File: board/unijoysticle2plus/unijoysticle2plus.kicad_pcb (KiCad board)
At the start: 2 copper layers, 35 parts, among them J1 DB9_Female, J2 DB9_Female, J3 Barrel_Jack, J4 Conn_01x03_Male, J5 USB_B_Micro, Q1 S8050, Q2 S8050, SW1 SW_Push, SW2 SW_SPST, SW3 SW_Push, SW4 SW_Push, U1 ESP32-WROOM-32D, U2 74LS05, U3 74LS05, U4 CP2102N-A01-GQFN24, U5 AP2114H-3_3TRG1

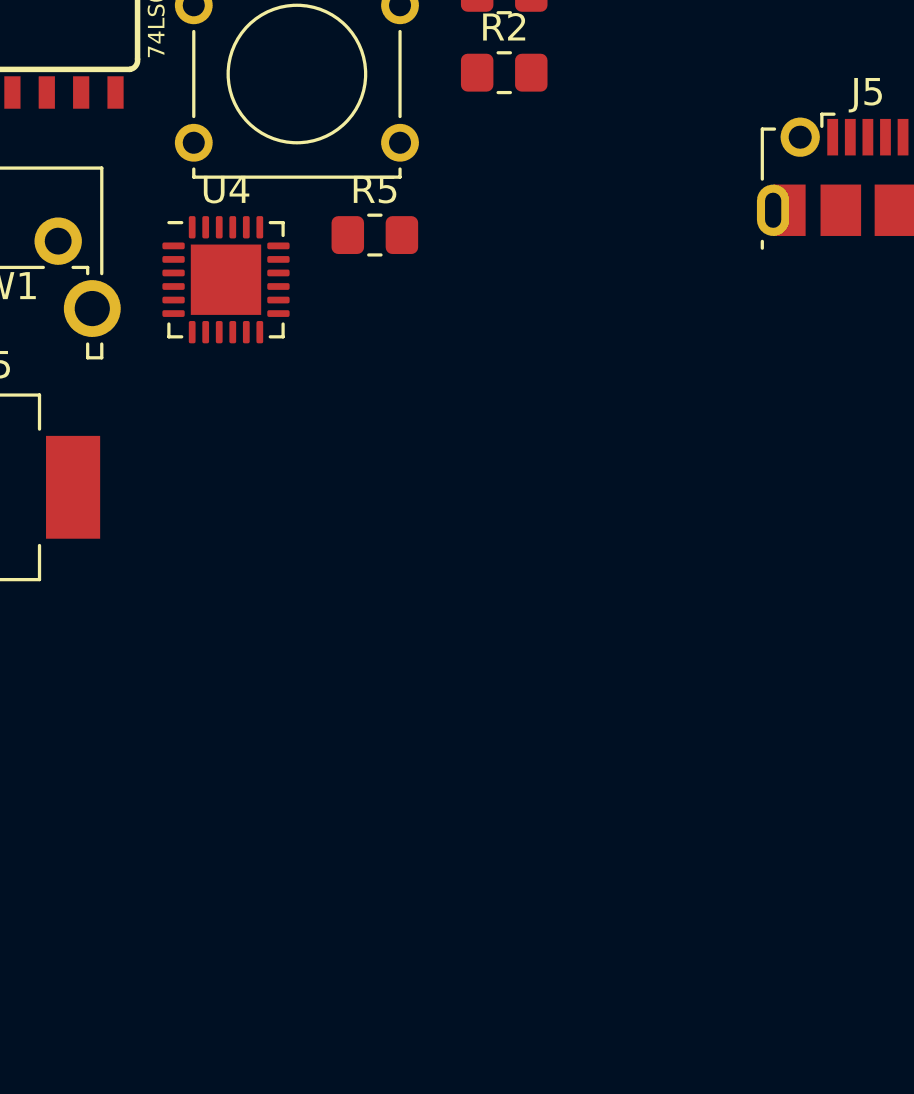
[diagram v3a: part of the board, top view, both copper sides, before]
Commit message: Firmware cleanup: remove obsolte files
Remove Changelog/License related to firmware
Remove code files from .gitignore
  Ignore fp-info-cache (kicad  file)
Update docs like pair_ds3 which points to Bluepad32

Regarding Unijoysticle2Plus: non important changes... this is still
pretty much WIP, so just ignore these changes
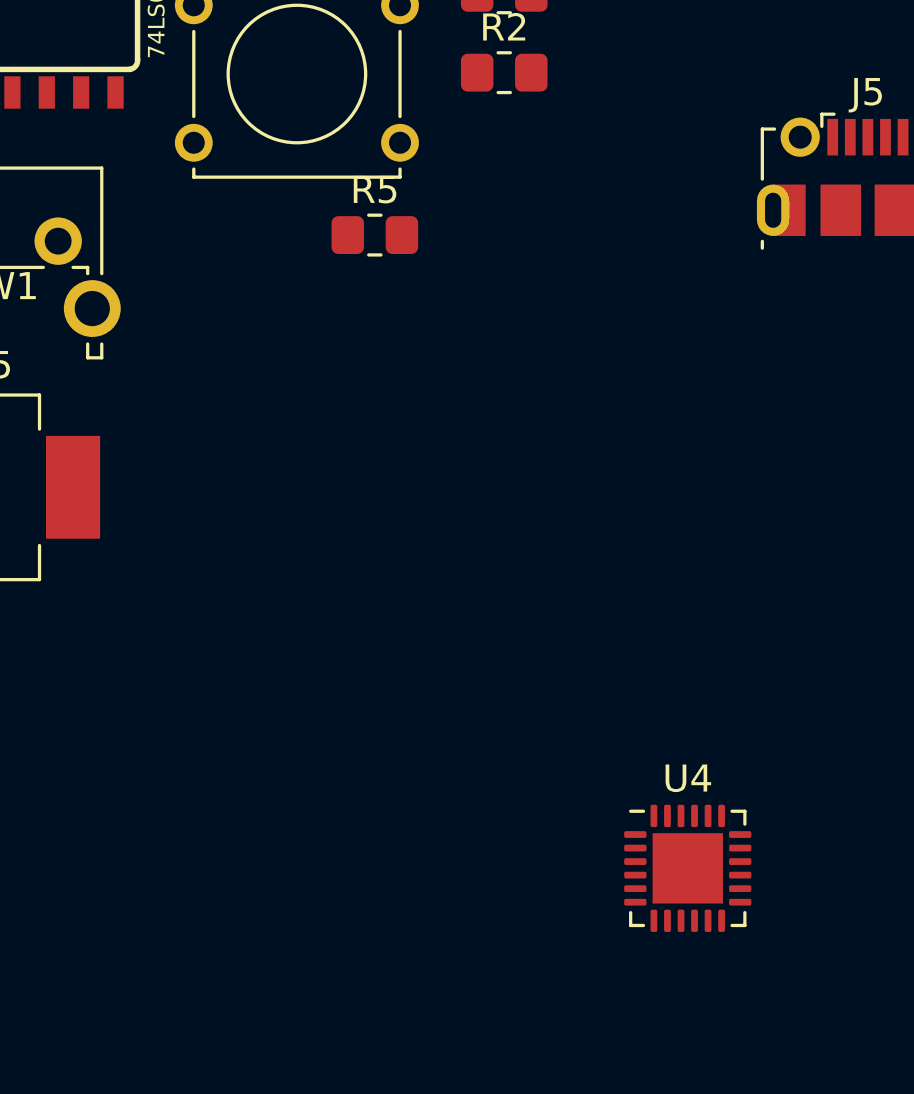
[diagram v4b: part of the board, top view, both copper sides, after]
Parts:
- moved U4 27.6 mm to (139.2, -14.2)

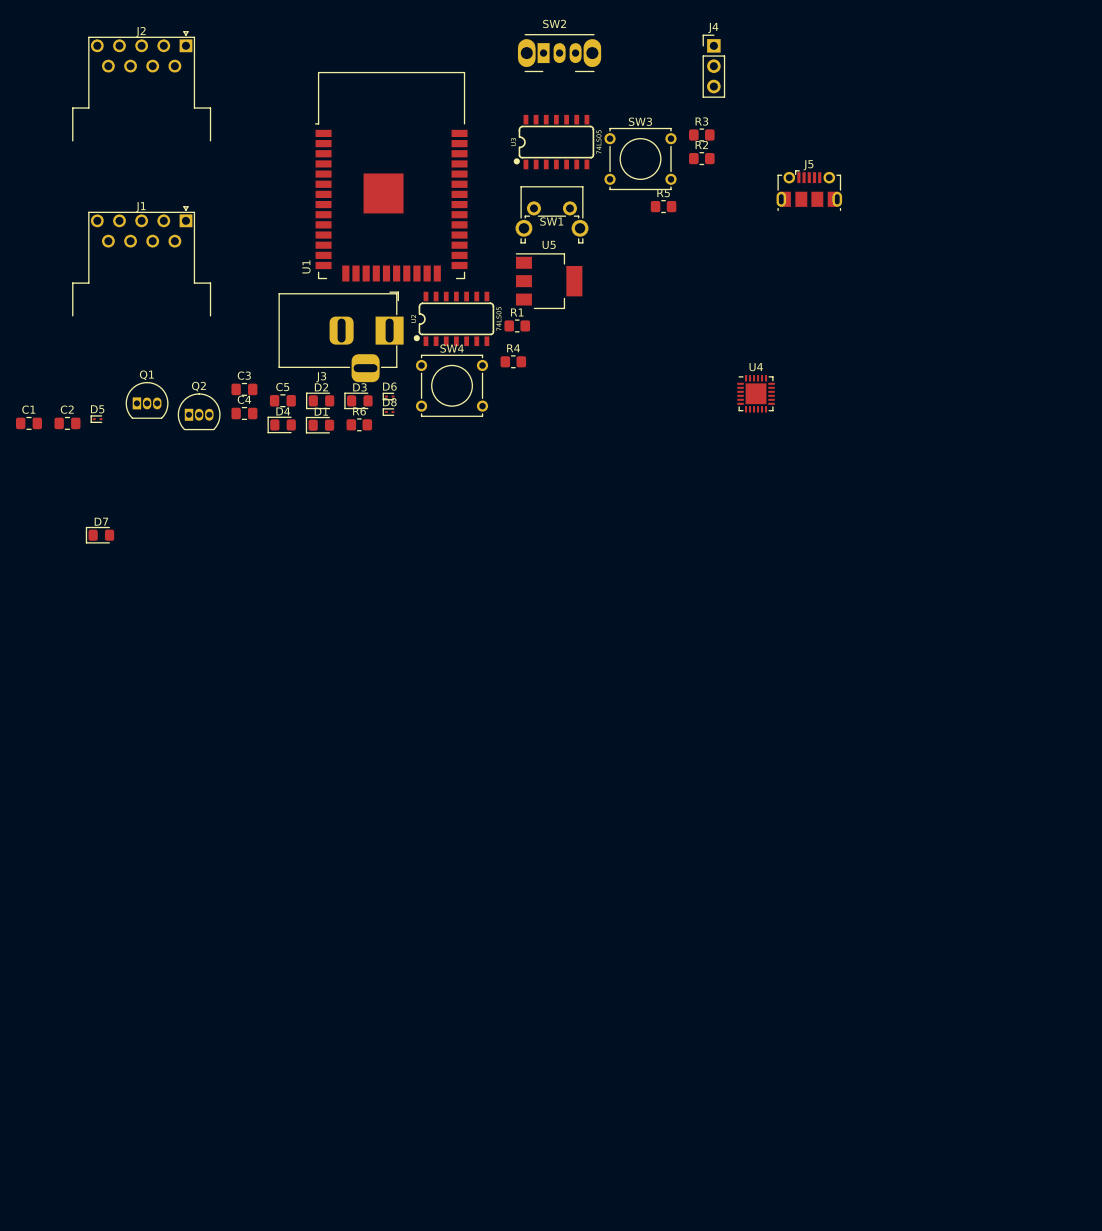
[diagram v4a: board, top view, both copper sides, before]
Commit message: unijoysticle2 plus: using ch340c (WIP)
After researching which could be the cheapest way to create a board that
could be assembled by JLCPCB, it seems that using CH340C is the way to
go:

- CH340C is an extended part, but doesn't require oscillator. Cost: $0.5
- CH340G is a basic part, but requires 12Mhz oscillar, which is an
  external part.
- CP210x, are all external parts and cost > $2

So, the design will include a CH340C.

Schematic is "ready", but layout is not.
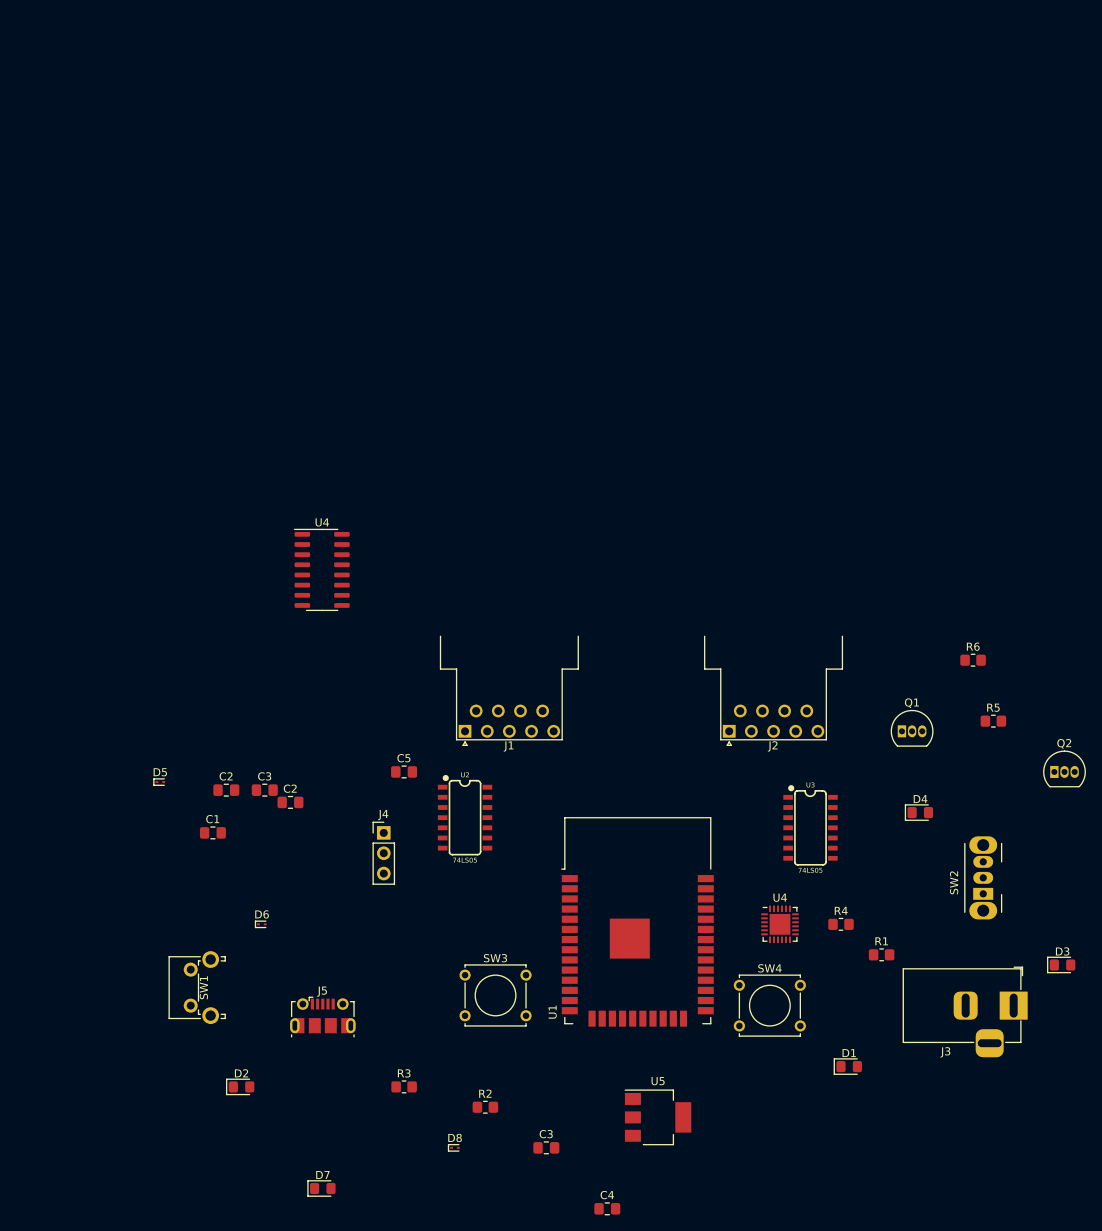
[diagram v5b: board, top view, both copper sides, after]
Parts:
- added C2: .1uF, Capacitor_SMD:C_0805_2012Metric_Pad1.18x1.45mm_HandSolder, F.Cu at (73.0, 35.3)
- added C3: .1uF, Capacitor_SMD:C_0805_2012Metric_Pad1.18x1.45mm_HandSolder, F.Cu at (77.8, 35.3)
- added U4: CH340C, Package_SO:SOIC-16_3.9x9.9mm_P1.27mm, F.Cu at (85.0, 7.77)
- moved R3 124.7 mm to (95.2, 72.4)
- moved R2 121.6 mm to (105.4, 74.9)
- moved J5 119.9 mm to (85.1, 63.5)
- moved SW2 118.6 mm to (167.6, 48.3), turned to 90 degrees
- moved Q2 117.0 mm to (176.5, 33.0)
- moved J3 114.9 mm to (171.4, 62.2)
- moved D3 112.6 mm to (177.6, 57.1)
- moved J2 109.3 mm to (135.9, 27.9), turned to 180 degrees
- moved C4 109.3 mm to (120.7, 87.6)
- moved SW1 108.5 mm to (68.6, 62.2), turned to 90 degrees
- moved J4 106.7 mm to (92.7, 40.6)
- moved SW3 106.1 mm to (102.9, 58.4)
- moved U5 105.4 mm to (127.0, 76.2)
- moved Q1 104.0 mm to (157.5, 27.9)
- moved D1 103.8 mm to (150.9, 69.8)
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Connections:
- C1 pad 2: GND -> +5V
- C4 pad 2: GND -> +5V
- C5 pad 2: GND -> +5V
- D1 pad 1: GND -> +5V
- D2 pad 1: GND -> +5V
- D5 pad 1: GND -> +5V
- D6 pad 1: GND -> +5V
- D6 pad 2: /USB_DP -> /USBD+
- D8 pad 1: GND -> +5V
- D8 pad 2: /USB_DN -> /USBD-
- J1 pad 5: (no net) -> /J1_POTY
- J1 pad 8: GND -> +5V
- J1 pad 9: (no net) -> /J1_POTX
- J2 pad 5: (no net) -> /J2_POTY
- J2 pad 8: GND -> +5V
- J2 pad 9: (no net) -> /J2_POTX
- J3 pad 2: GND -> +5V
- J5 pad 2: /USB_DN -> /USBD-
- J5 pad 3: /USB_DP -> /USBD+
- J5 pad 4: (no net) -> Net-(J5-Pad4)
- J5 pad 5: GND -> +5V
- J5 pad 6: GND -> +5V
- Q1 pad 3: (no net) -> /BOOT
- SW1 pad 1: GND -> +5V
- SW3 pad 1: GND -> +5V
- SW4 pad 2: GND -> +5V
- U1 pad 1: GND -> +5V
- U1 pad 15: GND -> +5V
- U1 pad 17: (no net) -> Net-(U1-Pad17)
- U1 pad 18: (no net) -> Net-(U1-Pad18)
- U1 pad 19: (no net) -> Net-(U1-Pad19)
- U1 pad 20: (no net) -> Net-(U1-Pad20)
- U1 pad 21: (no net) -> Net-(U1-Pad21)
- U1 pad 22: (no net) -> Net-(U1-Pad22)
- U1 pad 24: (no net) -> Net-(U1-Pad24)
- U1 pad 27: (no net) -> /GPIO_J1_POTY
- U1 pad 32: (no net) -> Net-(U1-Pad32)
- U1 pad 33: (no net) -> /GPIO_J2_POTX
- U1 pad 34: /RXD -> /ESP_RXD
- U1 pad 35: /TXD -> /ESP_TXD
- U1 pad 36: (no net) -> /GPIO_J2_POTY
- U1 pad 38: GND -> +5V
- U1 pad 39: GND -> +5V
- U1 pad 4: (no net) -> Net-(U1-Pad4)
- U1 pad 5: (no net) -> Net-(U1-Pad5)
- U1 pad 9: (no net) -> /GPIO_J1_POTX
- U2 pad 12: (no net) -> Net-(U2-Pad12)
- U2 pad 13: (no net) -> Net-(U2-Pad13)
- U2 pad 7: GND -> +5V
- U3 pad 12: (no net) -> Net-(U3-Pad12)
- U3 pad 13: (no net) -> Net-(U3-Pad13)
- U3 pad 7: GND -> +5V
- U5 pad 1: GND -> +5V

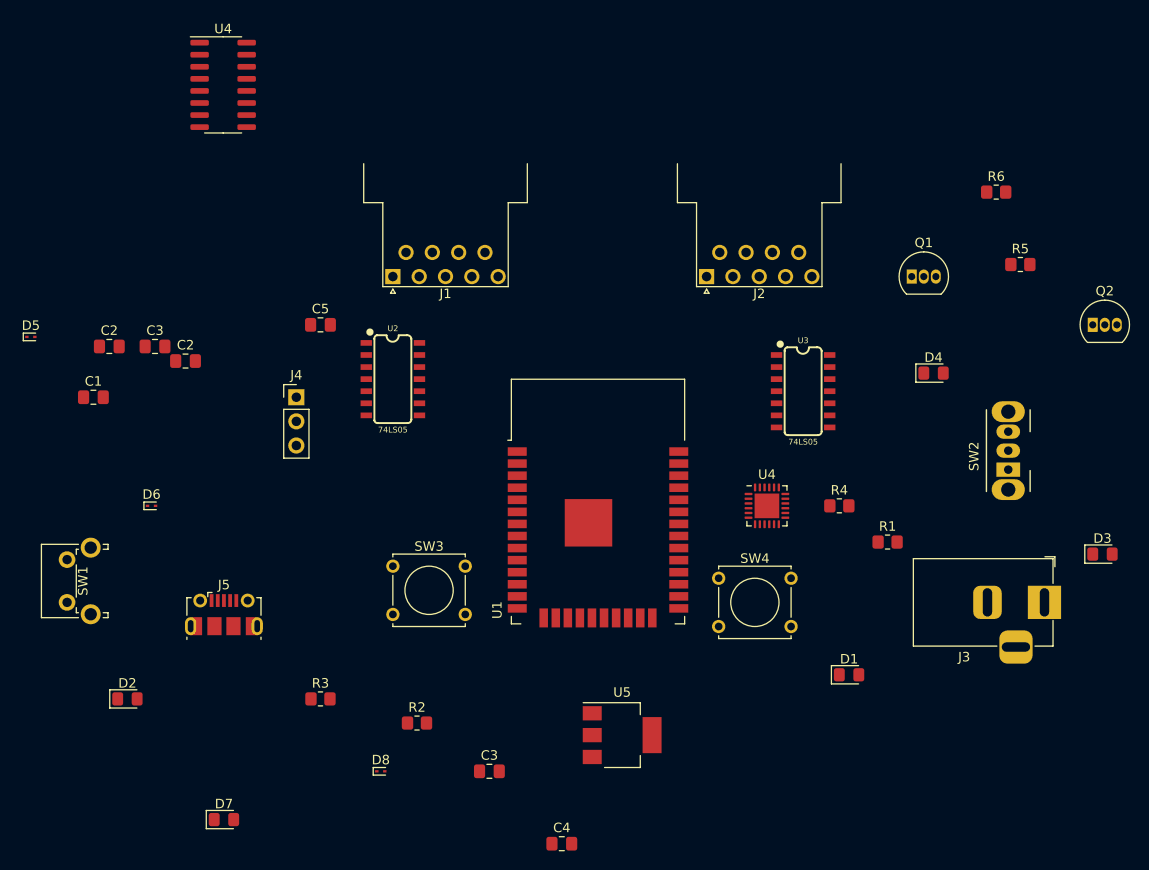
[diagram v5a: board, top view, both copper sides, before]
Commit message: unijoysticle2plus: auto-reset circuit fixed and minor fixes
Transistor had B/E/C wrong.
Correct package for push buttons for reset & boot.
Improved package for 7405 (renamed it from 74lc05 to 74hc05).

Reset layout. Not working on it yet since schematic is not ready yet
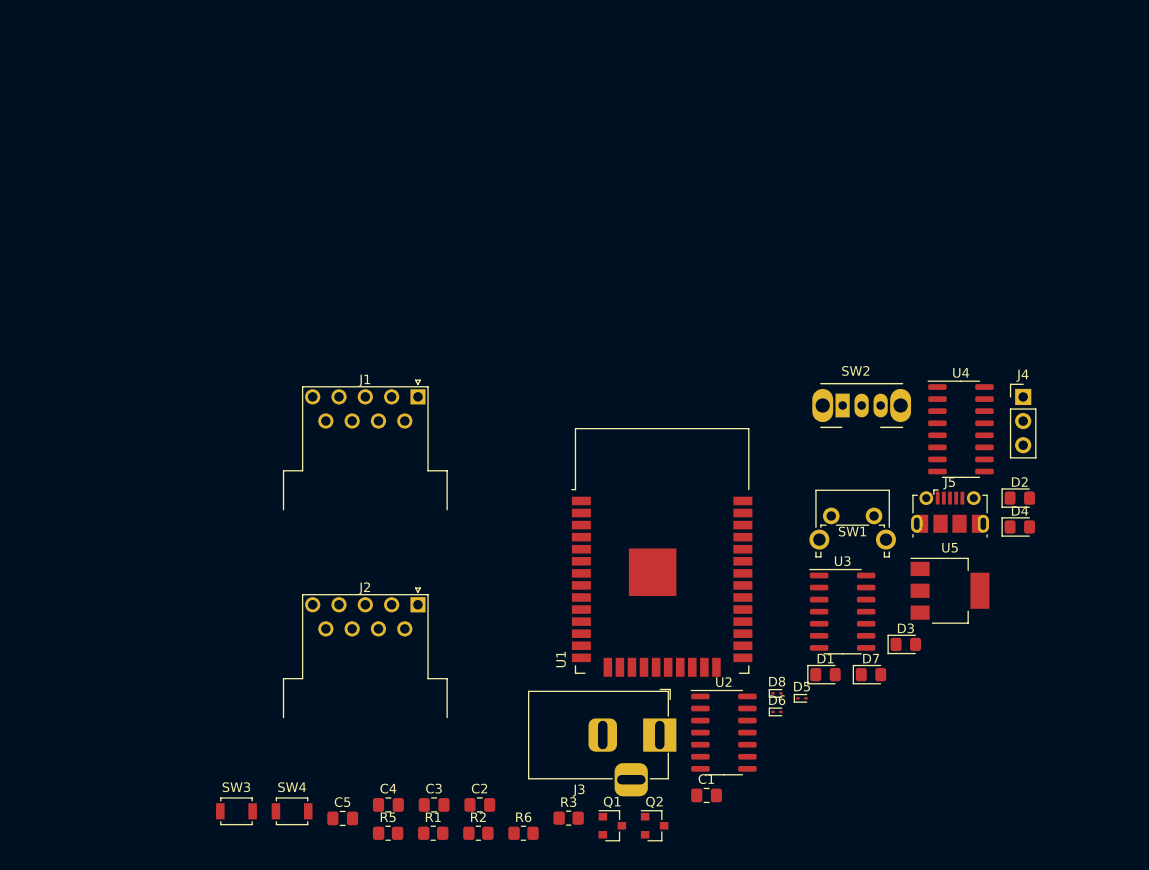
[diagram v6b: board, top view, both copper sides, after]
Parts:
- removed the C2 at (73.0, 35.3)
- removed the C2 at (81.0, 36.8)
- removed the C3 at (77.8, 35.3)
- removed the C3 at (113.0, 80.0)
- removed R4: 1k, Resistor_SMD:R_0805_2012Metric_Pad1.20x1.40mm_HandSolder
- removed the U4 at (85.0, 7.77)
- removed the U4 at (142.2, 52.1)
- added C2: .1uF, Capacitor_SMD:C_0805_2012Metric_Pad1.18x1.45mm_HandSolder, F.Cu at (112.0, 83.5)
- added C3: .1uF, Capacitor_SMD:C_0805_2012Metric_Pad1.18x1.45mm_HandSolder, F.Cu at (107.2, 83.5)
- added U4: CH340C, Package_SO:SOIC-16_3.9x9.9mm_P1.27mm, F.Cu at (162.7, 44.0)
- Q1, Q2: value S8050 -> MMSS8050-H-TP; footprint Package_TO_SOT_THT:TO-92_Inline -> Package_TO_SOT_SMD:SOT-23
- SW3, SW4: footprint Button_Switch_THT:SW_Tactile_Straight_KSA0Axx1LFTR -> Button_Switch_SMD:SW_SPST_B3U-1000P
- U2, U3: footprint Silicon-Standard:SO14 -> Package_SO:SOIC-14_3.9x8.7mm_P1.27mm
- moved D2 96.3 mm to (168.9, 51.3)
- moved D5 89.6 mm to (145.9, 72.3)
- moved R5 89.5 mm to (102.4, 86.5)
- moved R6 83.8 mm to (116.6, 86.5)
- moved SW1 80.9 mm to (149.0, 53.1), turned to 0 degrees
- moved J5 77.2 mm to (161.5, 52.7)
- moved C1 77.0 mm to (135.9, 82.5)
- moved J4 76.5 mm to (169.2, 40.6)
- moved Q2 70.0 mm to (130.4, 85.7)
- moved D7 69.8 mm to (153.2, 69.8)
- moved D6 69.3 mm to (143.3, 73.8)
- moved Q1 65.8 mm to (126.0, 85.7)
- moved R1 56.8 mm to (107.1, 86.5)
- moved C5 52.0 mm to (97.6, 85.0)
- moved U2 51.4 mm to (137.7, 75.9), turned to 0 degrees
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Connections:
- C1 pad 1: /RESET -> /ESP_RESET
- Q1 pad 1: /DTR_PROG -> Net-(Q1-Pad1)
- Q1 pad 2: Net-(Q1-Pad2) -> /RTS_PROG
- Q1 pad 3: /BOOT -> /ESP_RESET
- Q2 pad 1: /RESET -> Net-(Q2-Pad1)
- Q2 pad 2: Net-(Q2-Pad2) -> /DTR_PROG
- Q2 pad 3: /RTS_PROG -> /ESP_BOOT
- R3 pad 2: /RESET -> /ESP_RESET
- R5 pad 1: Net-(Q1-Pad2) -> Net-(Q1-Pad1)
- R5 pad 2: /RTS_PROG -> /DTR_PROG
- R6 pad 1: /DTR_PROG -> /RTS_PROG
- R6 pad 2: Net-(Q2-Pad2) -> Net-(Q2-Pad1)
- SW3 pad 2: /RESET -> /ESP_RESET
- U1 pad 3: /RESET -> /ESP_RESET
